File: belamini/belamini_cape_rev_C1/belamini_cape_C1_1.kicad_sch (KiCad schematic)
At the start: 21 parts, among them IC1 TSV524xIQ4T, IC2 TSV524xIQ4T, IC3 ADS8168, J1 Conn_01x10

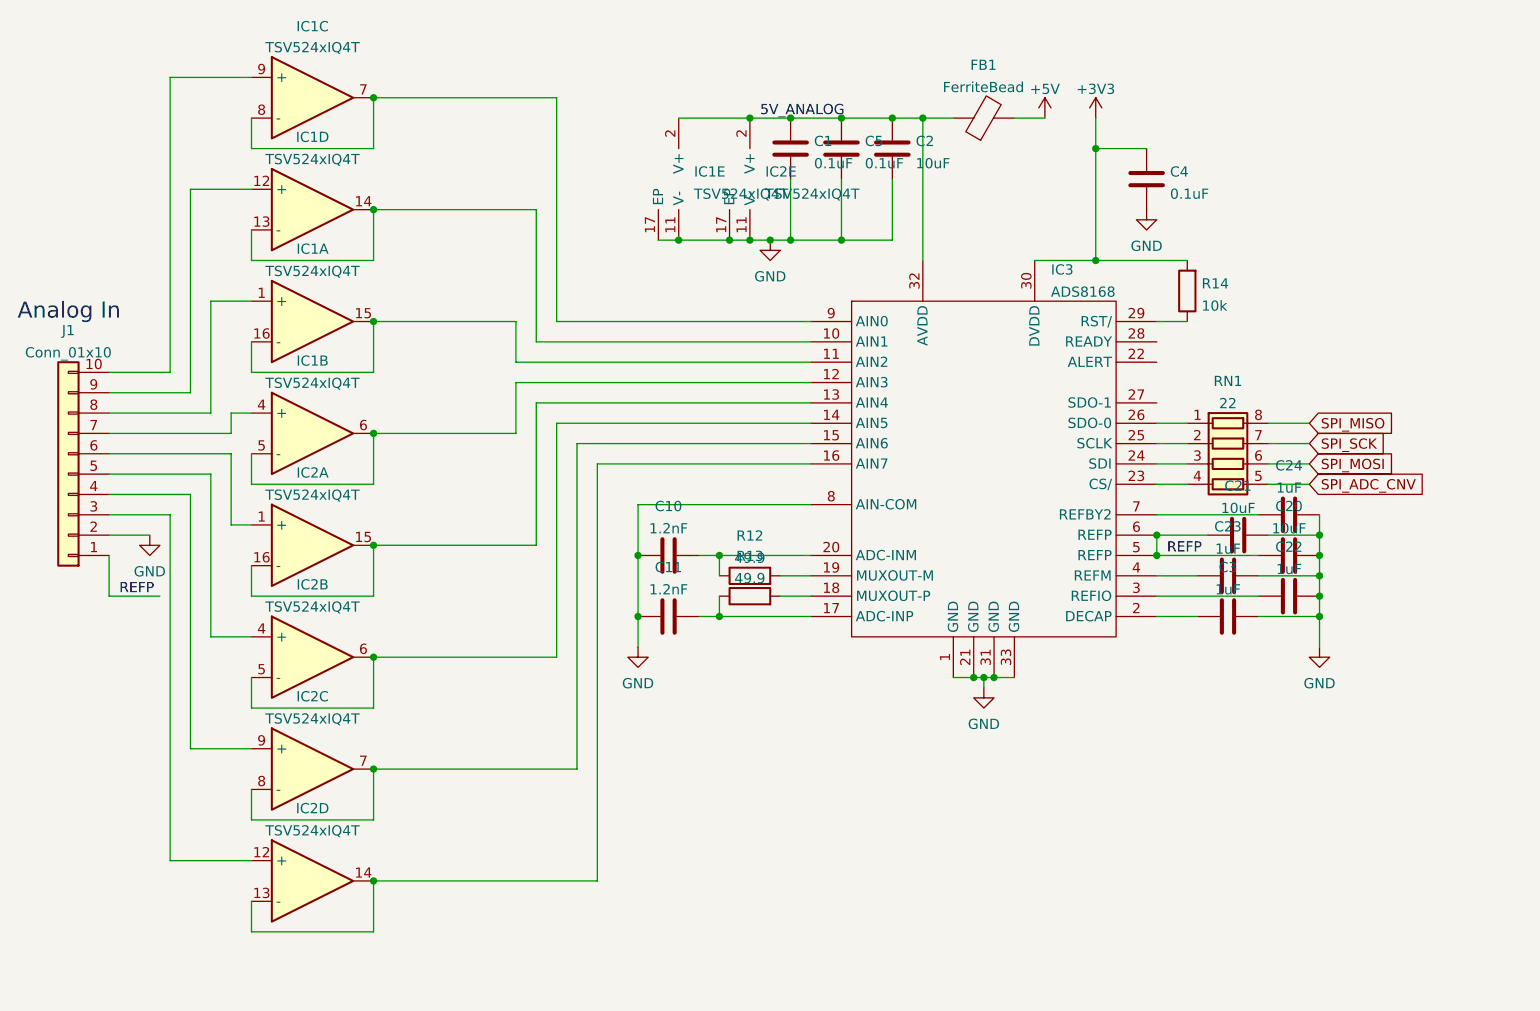
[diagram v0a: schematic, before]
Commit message: Add logo to Mini rev. C1, clean up schematic and add production files
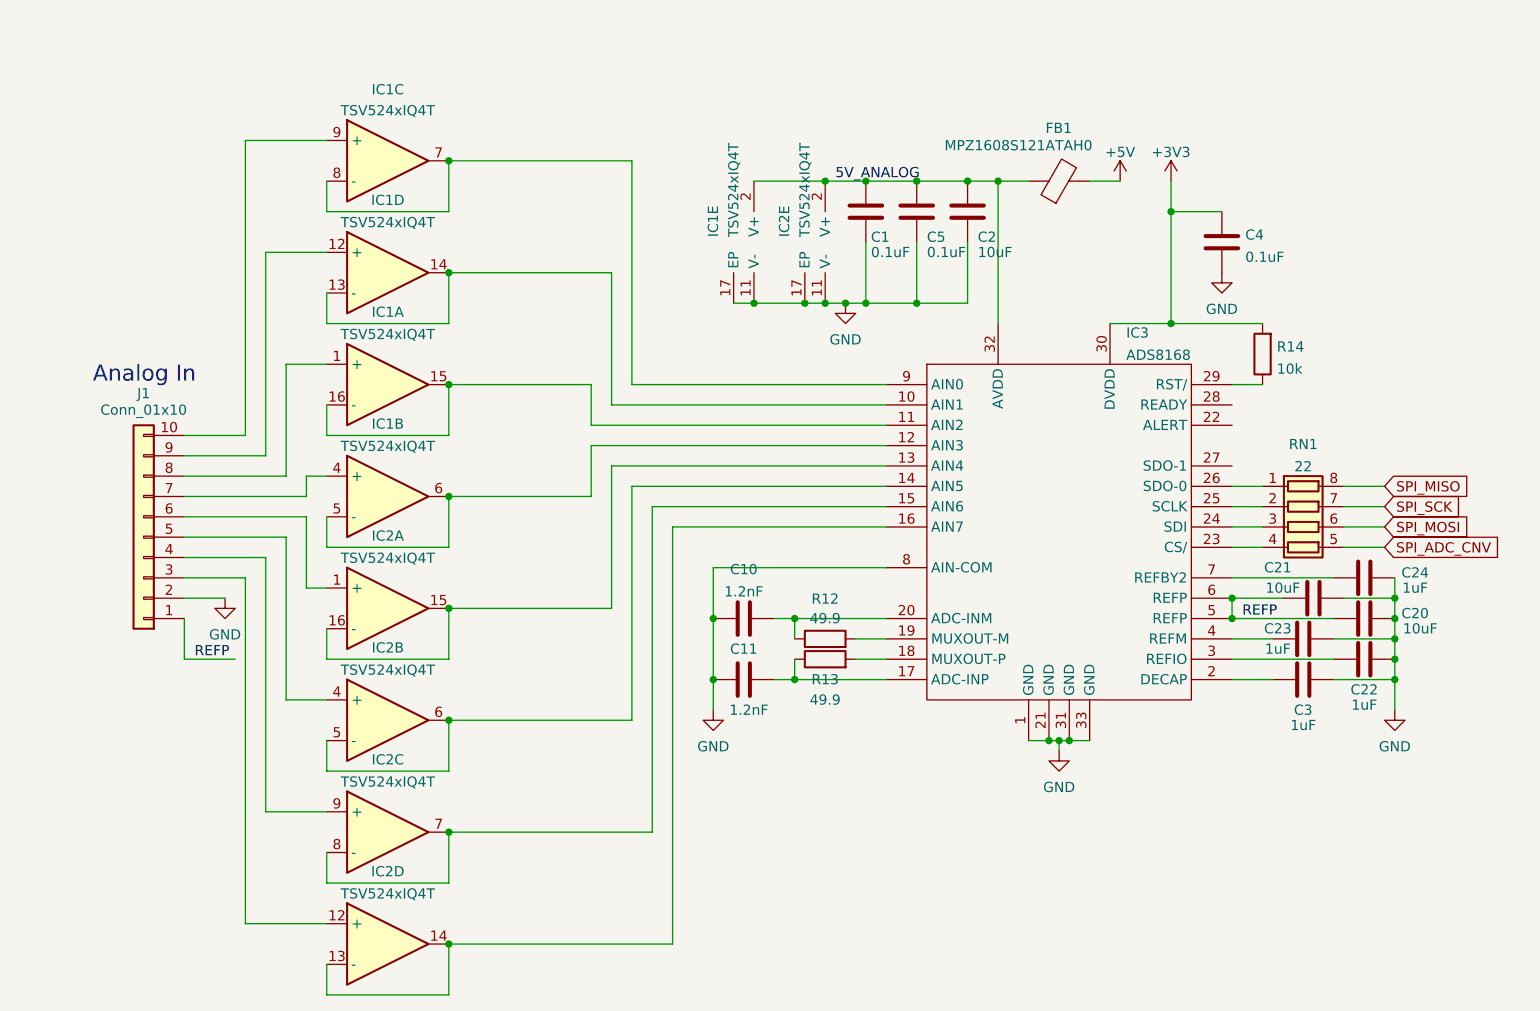
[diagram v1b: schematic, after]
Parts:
- FB1: value FerriteBead -> MPZ1608S121ATAH0
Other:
- company: (none) -> Augmented Instruments Ltd
- title: (none) -> Bela Mini
- moved on the sheet: C1, C10, C11, C2, C20, C21, C22, C23, C24, C3, C4, C5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
